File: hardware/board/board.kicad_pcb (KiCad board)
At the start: 2 copper layers, 70.1 x 22.5 mm, 40 parts, among them J1 Power, J10 OUT B3, J11 OUT B4, J2 IN A, J3 OUT A1, J4 OUT A2, J5 OUT A3, J6 OUT A4, J7 IN B, J8 OUT B1, J9 OUT B2, U1 OPA4991, U2 OPA4991, U3 LM358

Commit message: Update resistor values
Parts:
- R1, R2, R3, R4, R5, R6, R7, R8: value 100R -> 50R
- R10, R9: value 270R -> 1.5k

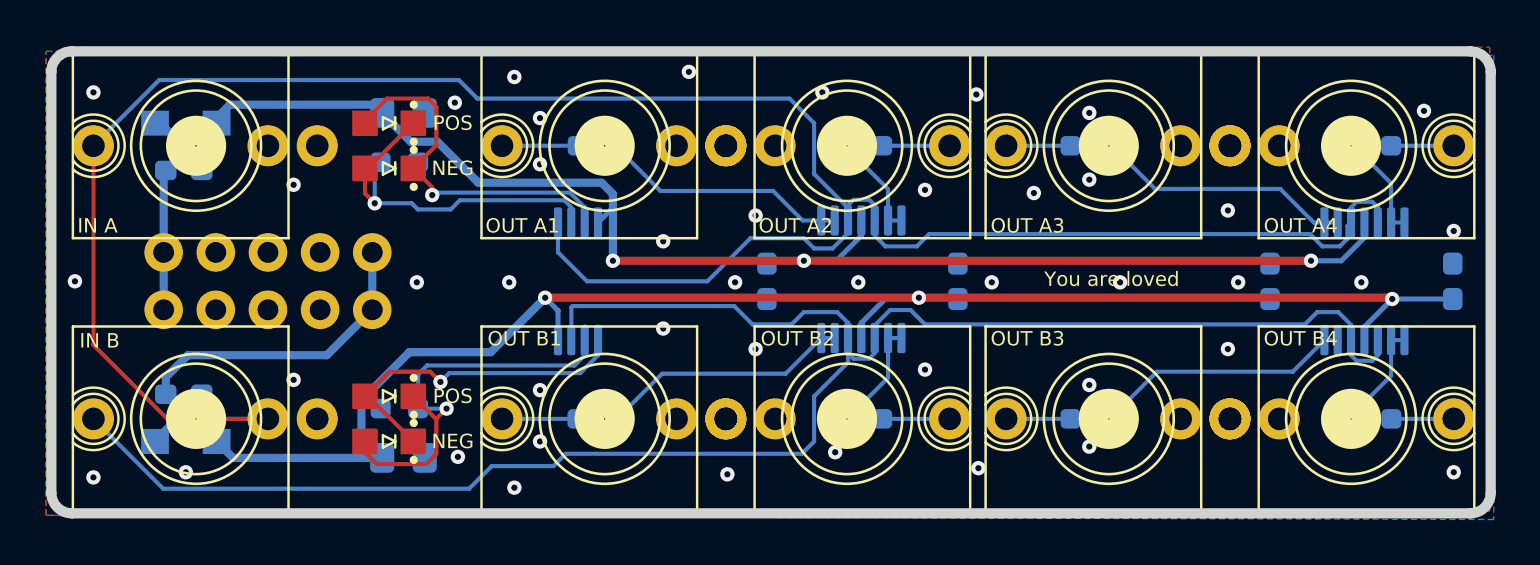
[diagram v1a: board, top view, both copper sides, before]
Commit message: Migrate to KiCAD 6, fix flipped C2
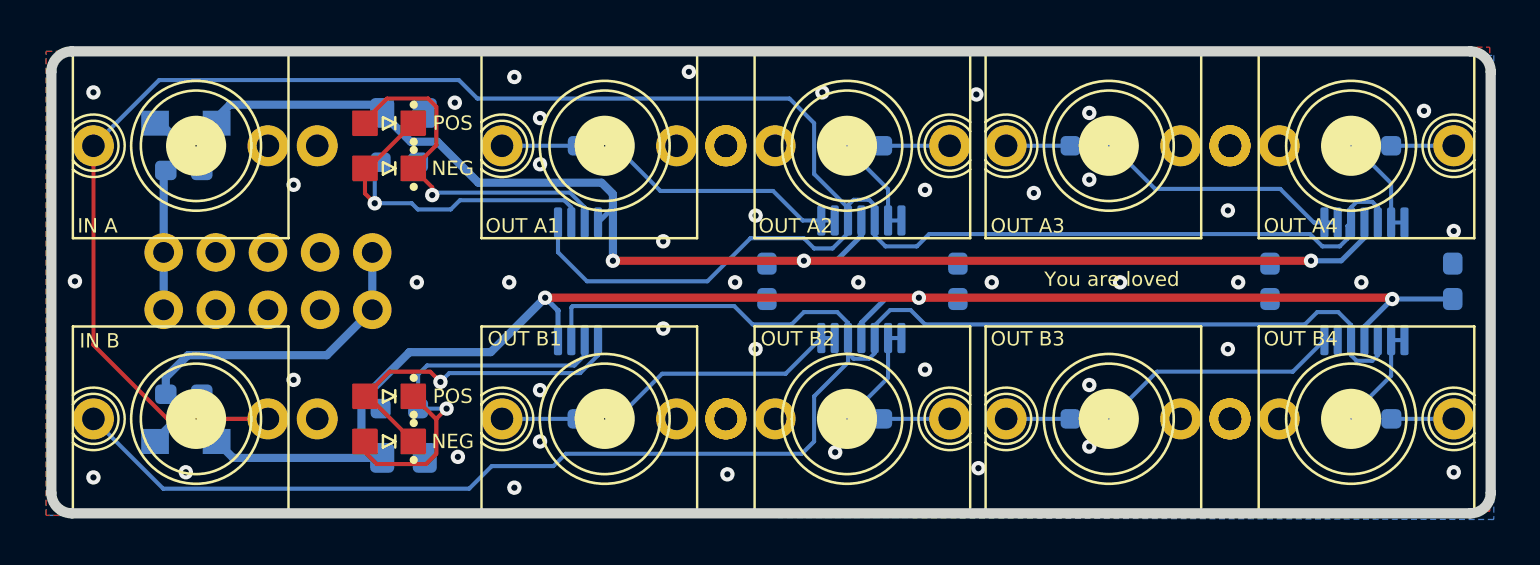
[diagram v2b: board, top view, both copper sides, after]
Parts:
- turned C2 to 180 degrees
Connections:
- C2 pad 1: -12V -> GND
- C2 pad 2: GND -> -12V
- J10 pad TN: Net-(J10-PadTN) -> unconnected-(J10-PadTN)
- J11 pad TN: Net-(J11-PadTN) -> unconnected-(J11-PadTN)
- J3 pad TN: Net-(J3-PadTN) -> unconnected-(J3-PadTN)
- J4 pad TN: Net-(J4-PadTN) -> unconnected-(J4-PadTN)
- J5 pad TN: Net-(J5-PadTN) -> unconnected-(J5-PadTN)
- J6 pad TN: Net-(J6-PadTN) -> unconnected-(J6-PadTN)
- J8 pad TN: Net-(J8-PadTN) -> unconnected-(J8-PadTN)
- J9 pad TN: Net-(J9-PadTN) -> unconnected-(J9-PadTN)
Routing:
- net Net-(J7-PadT): track 90.8 -> 89.5 mm
- net Net-(D5-Pad1): track 21.5 -> 20.2 mm
- net Net-(D5-Pad2): track 17.4 -> 16.4 mm
- net -12V: track 77.3 -> 76.5 mm
- net Net-(J2-PadT): track 111.4 -> 110.8 mm
- net Net-(D3-Pad1): track 18.0 -> 17.5 mm
- net Net-(D3-Pad2): track 18.3 -> 17.7 mm
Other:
- net class 12V removed
- net class 3.3V removed
- net class Absolute minimum removed
- net class Analog removed
- net class Default removed

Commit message: Board revision 3
Schematic:
- Migrated to new Winterbloom page layout
- Split into power and mult schematics
- Updated all symbols
- Added sourcing information for all items

PCB:
- Migrated to new Winterbloom page layout
- Updated all footprints
- Tweaked routing
- Updated all text to match current practices

Note:
- No values or placement locations were changed, this revision is largely cosmetic.
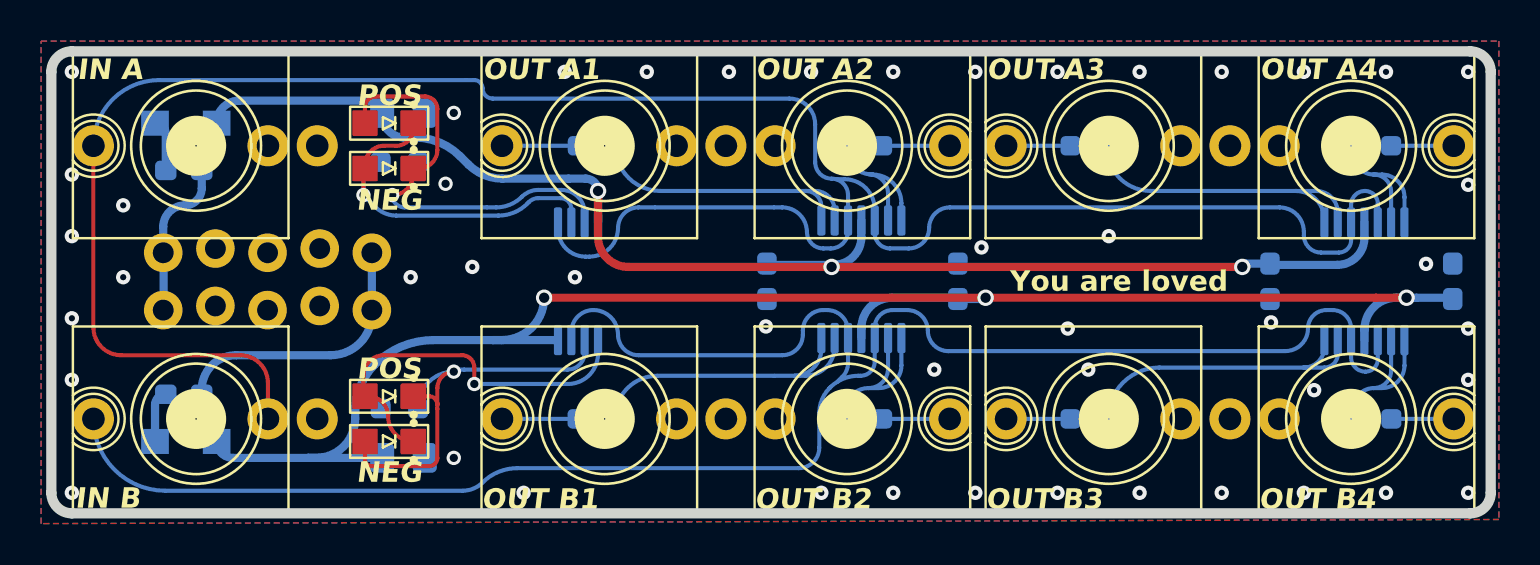
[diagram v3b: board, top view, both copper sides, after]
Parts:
- removed the G*** at (157.6, 119.8)
- added ?: , Graphics, B.Cu at (149.2, 110.8)
- added G***: LOGO, winterbloom:Symbol_Winterbloom_25mm, B.Cu at (157.8, 119.8)
- C1, C2: value 10uF -> 10u; footprint Capacitor_SMD:C_0805_2012Metric_Pad1.18x1.45mm_HandSolder -> winterbloom:C_0805_HandSolder
- C3, C4, C5, C6: value 0.1uF -> 100n; footprint Capacitor_SMD:C_0603_1608Metric_Pad1.08x0.95mm_HandSolder -> winterbloom:C_0603_HandSolder
- D1, D2: value BARRIER -> 30V; footprint winterbloom:DIODE_SOD-123_SOD-123F -> winterbloom:D_SOD-123+SOD-123F
- FB1, FB2: value BEAD -> 1k @ 100MHz; footprint Inductor_SMD:L_0603_1608Metric_Pad1.05x0.95mm_HandSolder -> winterbloom:L_0603_HandSolder
- J1: footprint winterbloom:Eurorack_Power -> winterbloom:Eurorack_Power_2x5_Shrouded_Lock
- J10, J2, J3, J5, J7, J8: footprint winterbloom:WQP-WQP518MA-skinny -> winterbloom:AudioJack_WQP518MA_Compact_S
- J11, J4, J6, J9: footprint winterbloom:WQP-WQP518MA-skinny -> winterbloom:AudioJack_WQP518MA_No_S
- R1, R2, R3, R4, R5, R6, R7, R8: value 50R -> 51R; footprint Resistor_SMD:R_0603_1608Metric_Pad0.98x0.95mm_HandSolder -> winterbloom:R_0603_HandSolder
- R10, R9: value 1.5k -> 1k5; footprint Resistor_SMD:R_0603_1608Metric_Pad0.98x0.95mm_HandSolder -> winterbloom:R_0603_HandSolder
- U3: value LM358 -> LM358PWR
- moved J1 5.22 mm to (116.1, 112.7)
- moved REF** 2.96 mm to (154.4, 111.4)
- turned FB1 to 0 degrees
- turned FB2 to 0 degrees
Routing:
- net Net-(J7-Tip): track 89.5 -> 96.0 mm
- net Net-(J2-Tip): track 110.8 -> 117.2 mm
- net -12V: track 76.5 -> 82.5 mm
- net Net-(D3-A): track 17.7 -> 21.4 mm
- net Net-(U1C--): track 5.42 -> 8.72 mm
- net Net-(U1D--): track 12.2 -> 15.5 mm
- net Net-(U2A--): track 12.5 -> 15.8 mm
- net Net-(U2C--): track 4.95 -> 8.12 mm
- net Net-(U2B--): track 5.14 -> 8.03 mm
- net Net-(U2D--): track 12.7 -> 15.4 mm
- net Net-(U1B--): track 5.16 -> 7.86 mm
- net Net-(D5-A): track 16.4 -> 19.1 mm
- net Net-(U1A--): track 12.2 -> 14.7 mm
- net Net-(FB1-Pad2): track 15.0 -> 13.4 mm
- net Net-(D3-K): track 17.5 -> 18.7 mm
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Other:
- board text added: "${TITLE} ${REVISION} ${ISSUE_DATE} ${COMMENT2} ${COMMENT3}"
- board text removed: "*"
- board text removed: "CERN-OHL-P V2 hydrogen.wntr.dev"
- board text removed: "Hydrogen v2 10/7/2021"
